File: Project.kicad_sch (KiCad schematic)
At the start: 25 parts, among them J1 Screw_Terminal_01x02, J2 Screw_Terminal_01x02, J3 Conn_01x04_Socket, Q1 BT136-500, U1 AMS1117-3.3, U2 ESP32-WROOM-32, U3 MOC3021M, U4 MCT2E

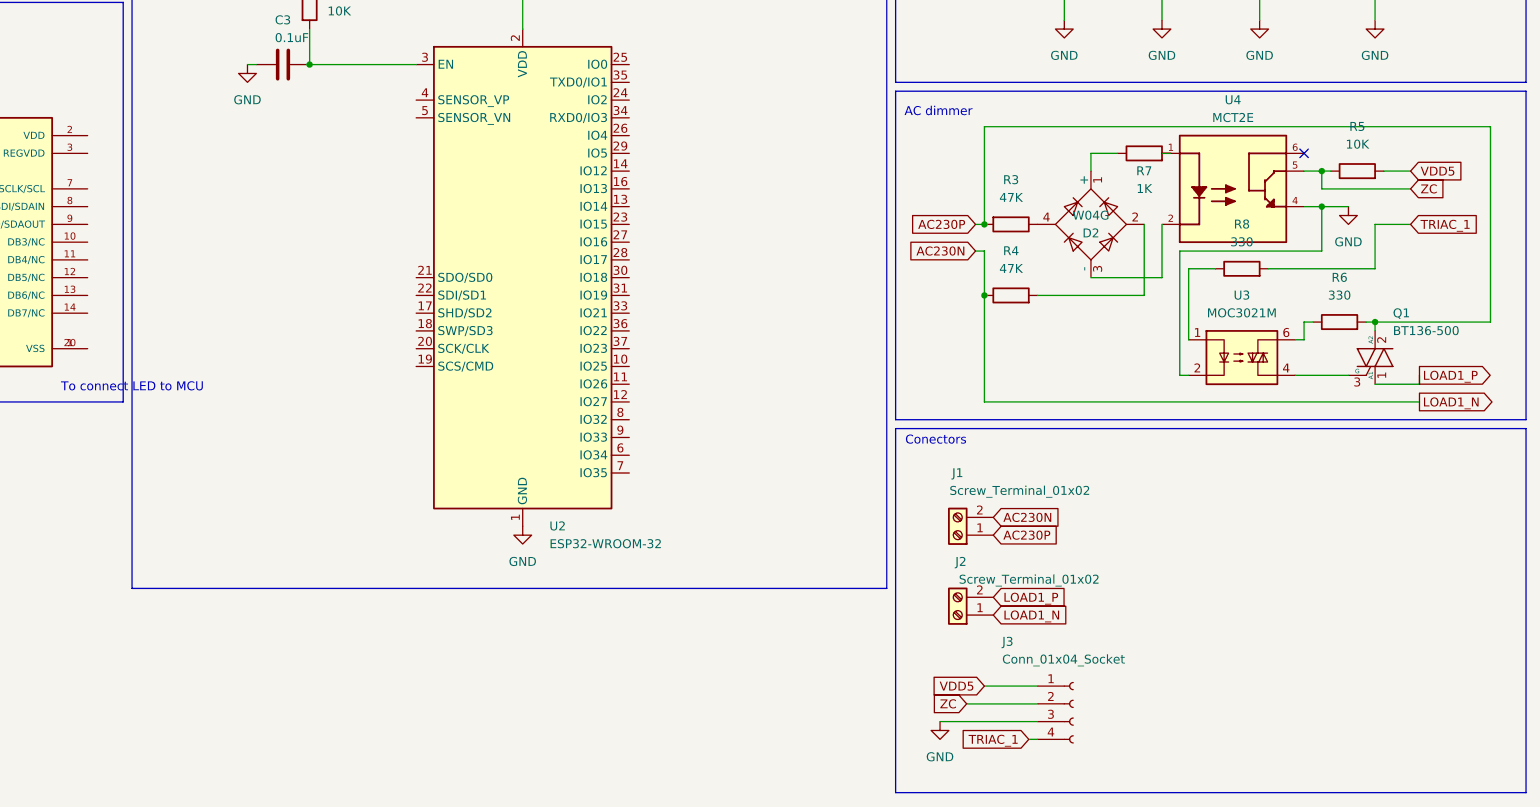
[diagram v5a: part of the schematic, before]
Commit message: Rotary encoders added
Added 2 rotary encoders
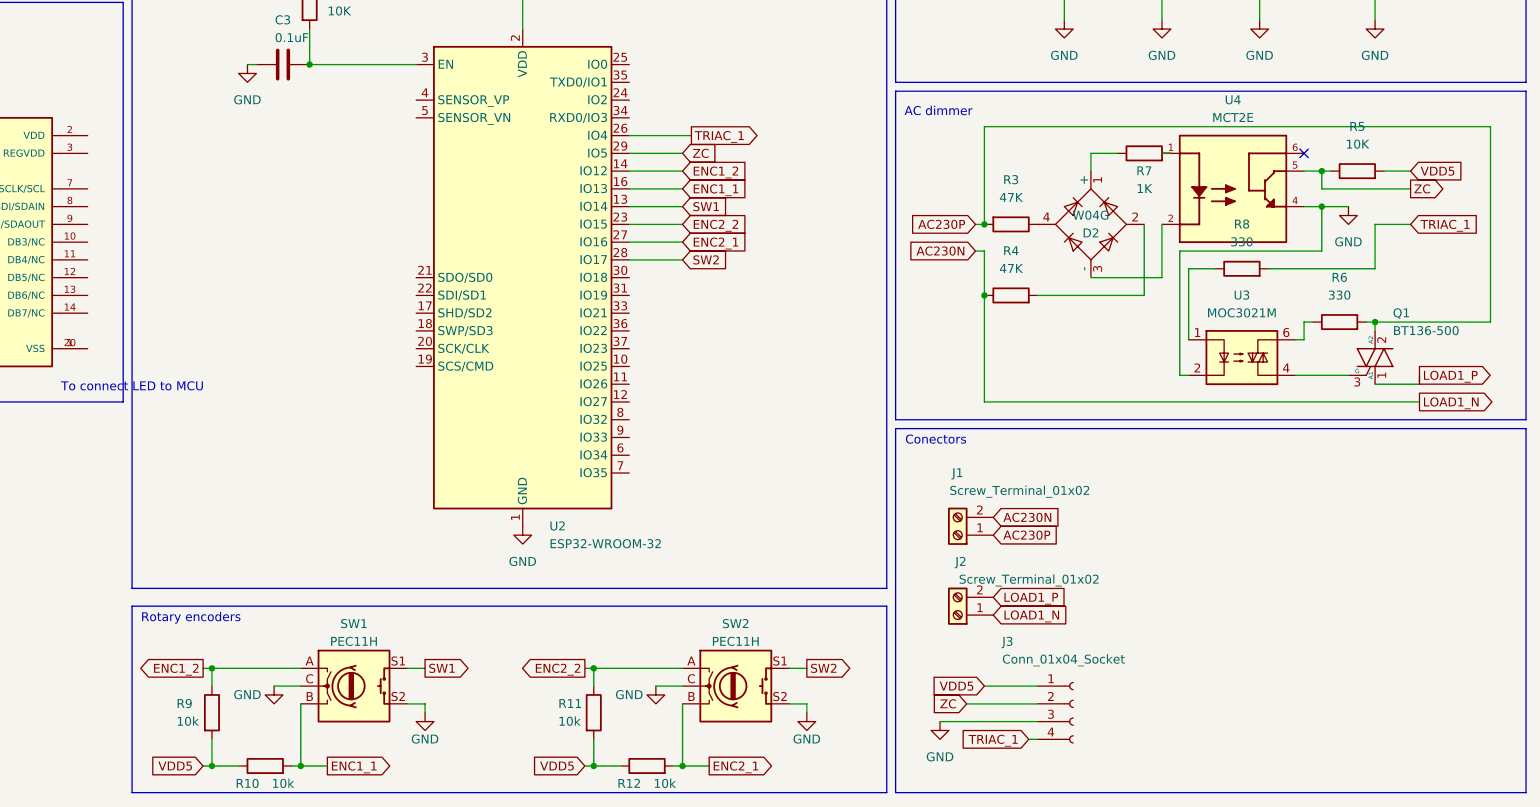
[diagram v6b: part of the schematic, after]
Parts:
- added R10, R11, R12, R9: 10k, symbol Device:R
- added SW1, SW2: PEC11H, symbol Device:RotaryEncoder_Switch
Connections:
- net GND: now also SW1.C, SW1.S2, SW2.C, SW2.S2
- net TRIAC_1: now also U2.26 (IO4)
- net VDD5: now also R10.1, R11.2, R12.1, R9.2
- net ZC: now also U2.29 (IO5)
- net SW1: now reaches U2.13 (IO14)
- net SW1: now also SW1.S1
- net ENC1_2: now reaches U2.14 (IO12)
- net ENC1_2: now also R9.1, SW1.A
- net ENC1_1: now reaches U2.16 (IO13)
- net ENC1_1: now also R10.2, SW1.B
- net ENC2_2: now reaches U2.23 (IO15)
- net ENC2_2: now also R11.1, SW2.A
- net ENC2_1: now reaches U2.27 (IO16)
- net ENC2_1: now also R12.2, SW2.B
- net SW2: now reaches U2.28 (IO17)
- net SW2: now also SW2.S1
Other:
- note added: "Rotary encoders"

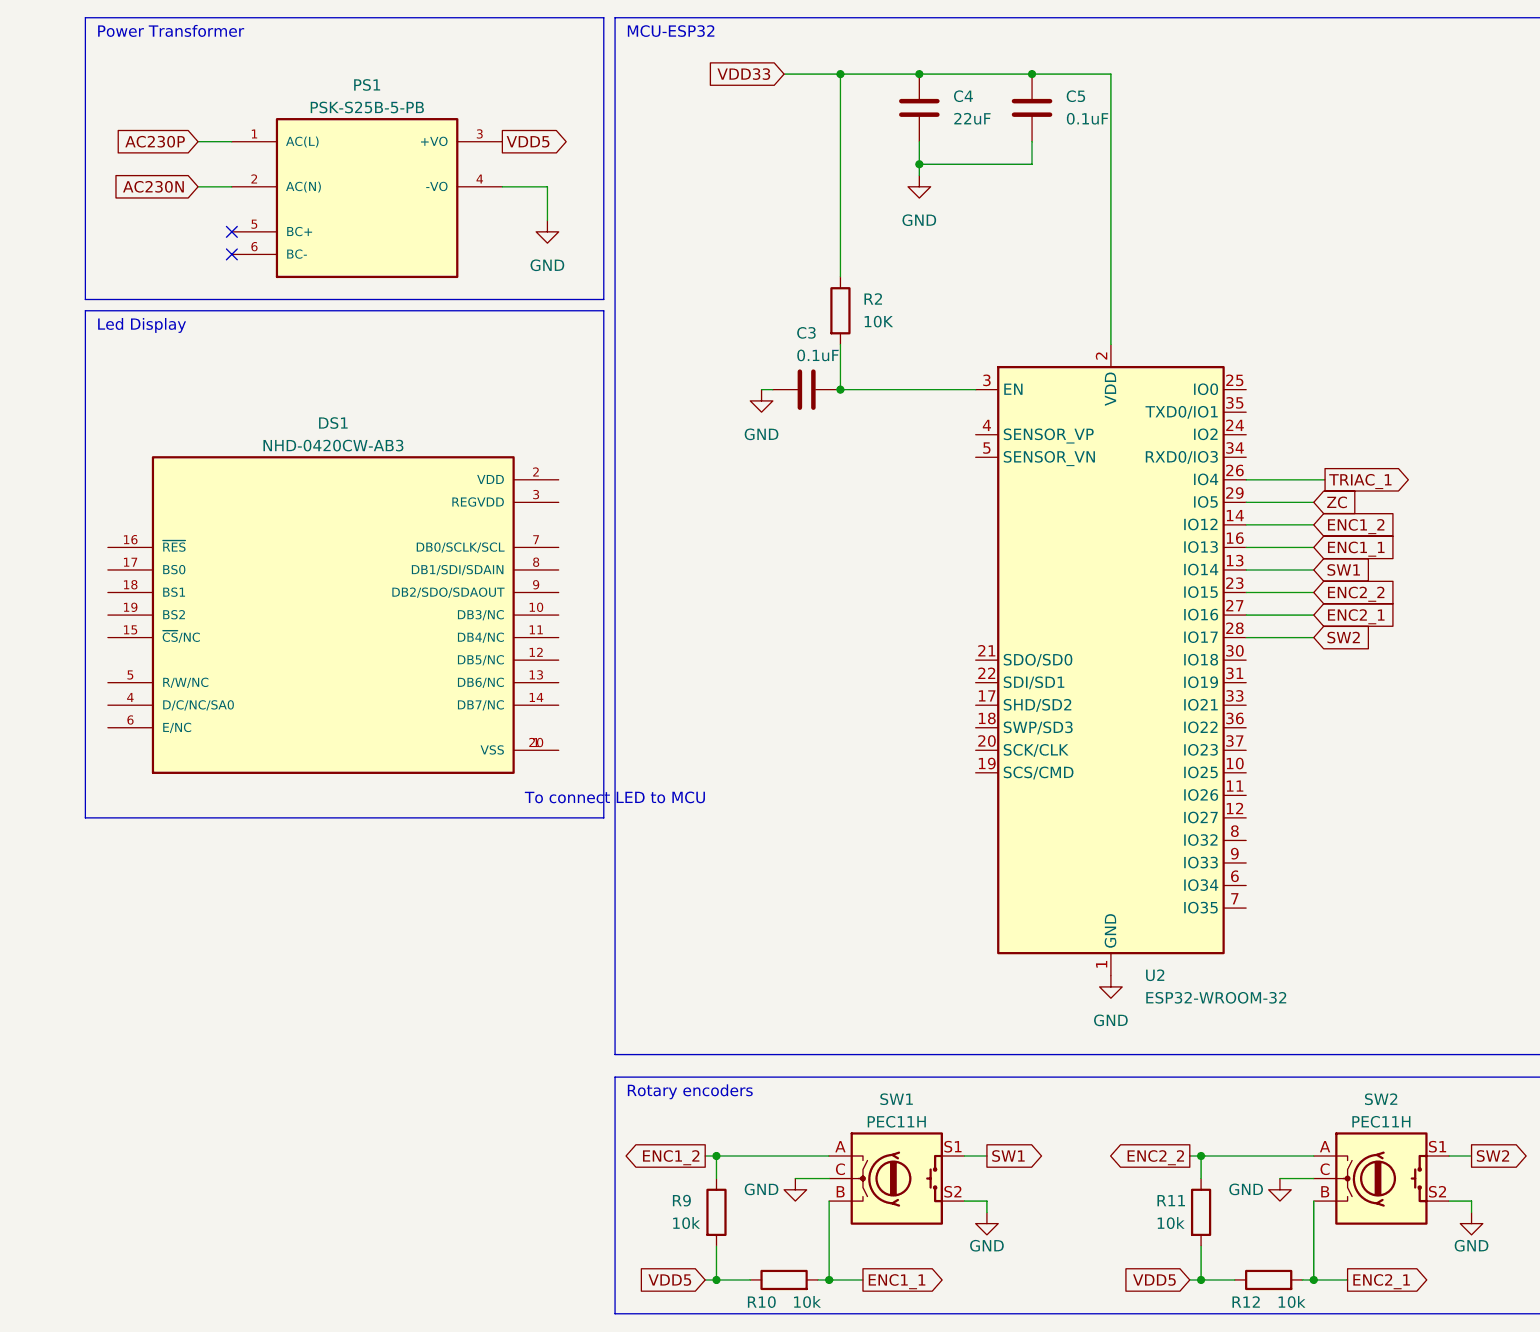
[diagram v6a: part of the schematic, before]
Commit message: Added microphone
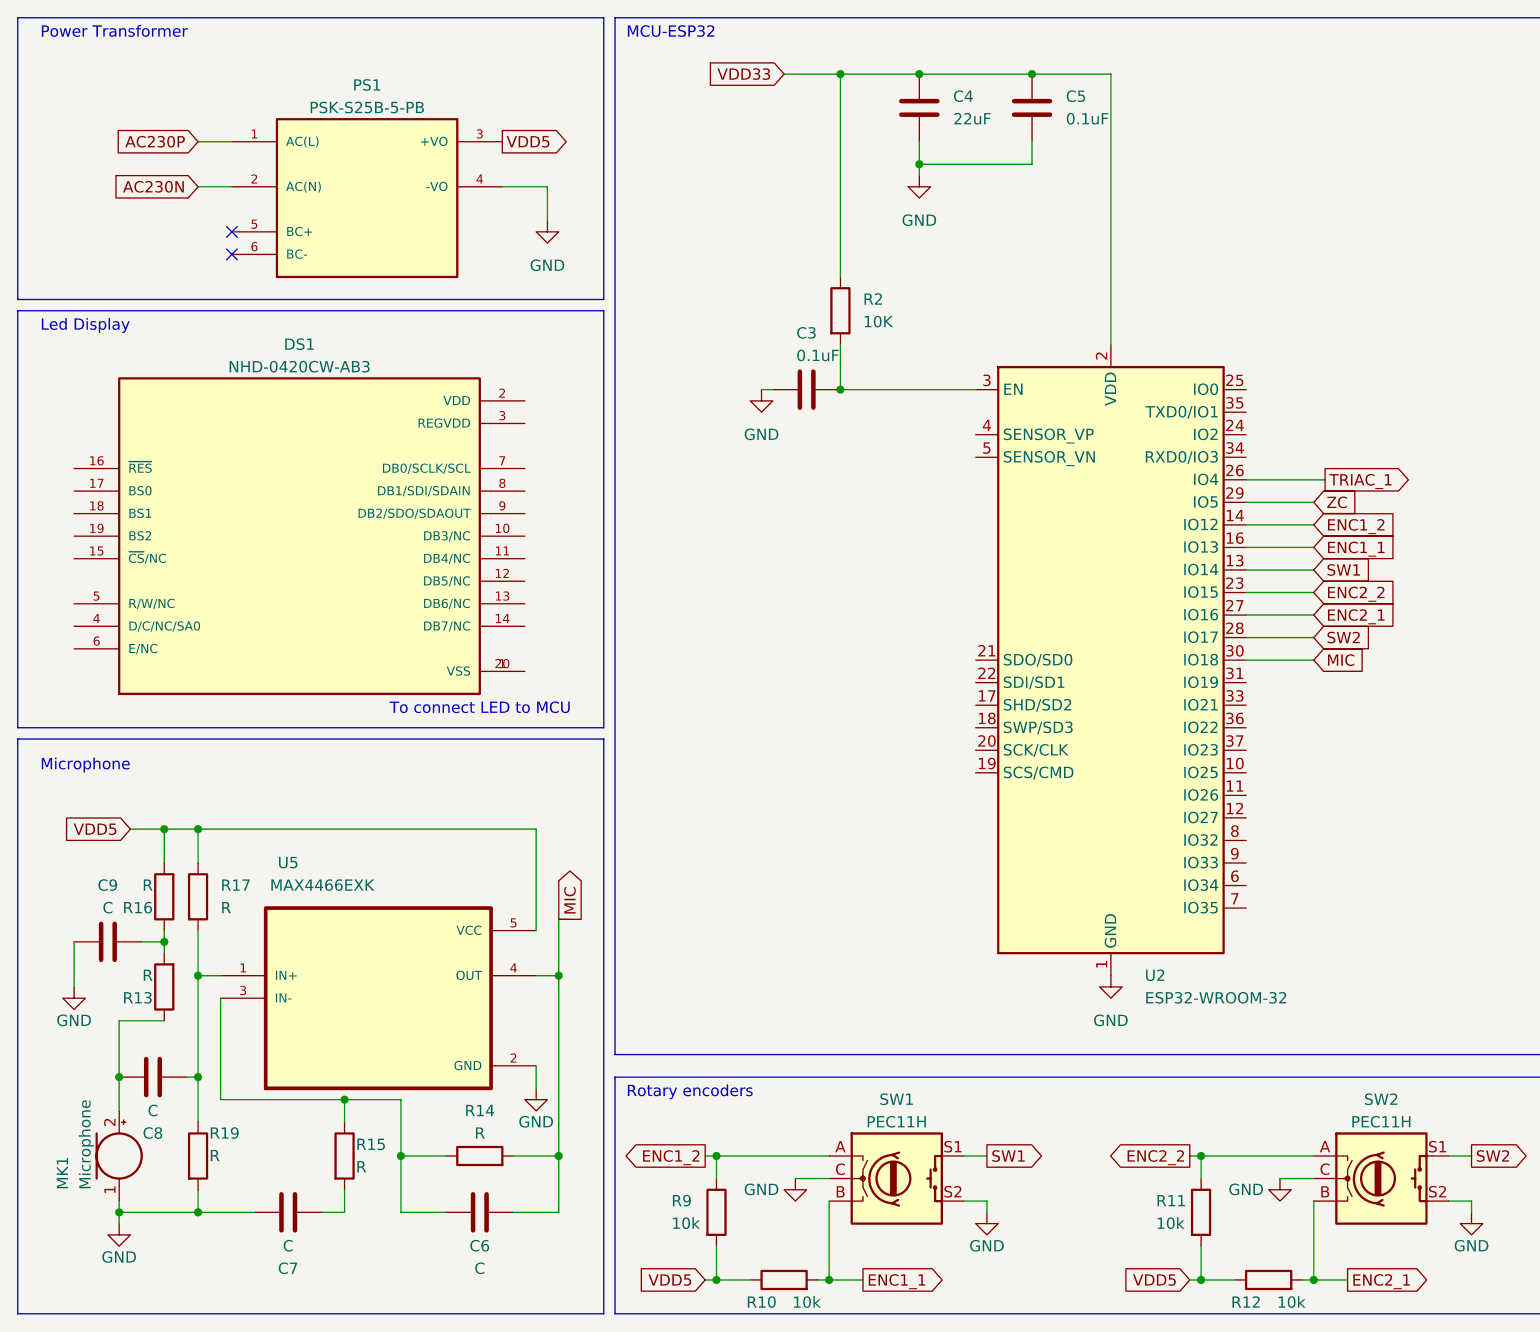
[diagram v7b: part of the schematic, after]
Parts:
- added C6, C7, C8, C9: C, symbol Device:C
- added MK1: Microphone, symbol Device:Microphone
- added R13, R14, R15, R16, R17, R19: R, symbol Device:R
- added U5: MAX4466EXK, MAX4466EXK:SOT65P210X110-5N, symbol MAX4466EXK:MAX4466EXK
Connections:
- net GND: now also C7.1, C9.2, MK1.1 (-), R19.2, U5.2 (GND)
- net VDD5: now also R16.2, R17.1, U5.5 (VCC)
- net MIC: now reaches U2.30 (IO18)
- net MIC: now also C6.1, R14.2, U5.4 (OUT)
- new net: C9.1, R13.2, R16.1
- new net: C8.1, MK1.2 (+), R13.1
- new net: C8.2, R17.2, R19.1, U5.1 (IN+)
- new net: C7.2, R15.2
- new net: C6.2, R14.1, R15.1, U5.3 (IN-)
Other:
- note added: "Microphone"
- moved on the sheet: DS1
